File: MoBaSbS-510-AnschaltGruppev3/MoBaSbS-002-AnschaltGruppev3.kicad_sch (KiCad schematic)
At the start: 37 parts, among them IC1 TJA1057BT, IC2 SP3485EN-L_TR, IC3 MCP2518FDT-E_SL, J1 RJ45, J2 RJ45, J3 Conn_02x03_Odd_Even, J4 Conn_01x03, J5 Conn_02x05_Counter_Clockwise, J6 Conn_01x04, J7 Conn_01x04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

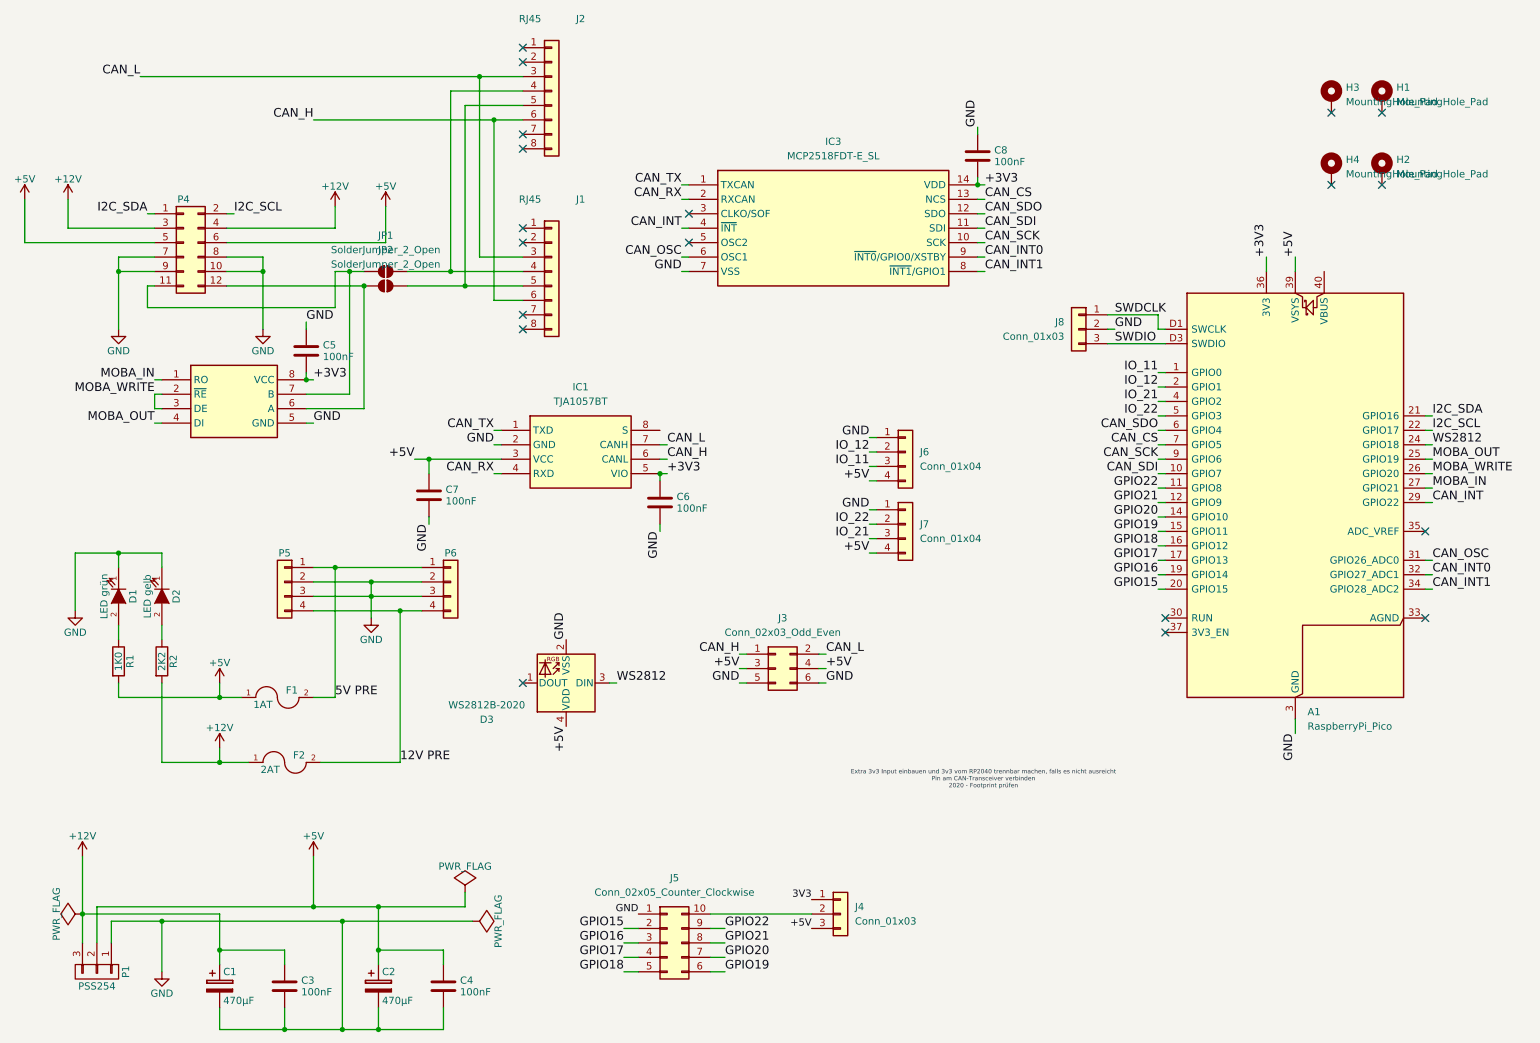
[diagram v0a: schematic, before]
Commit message: Finished up PCBs, added stencil
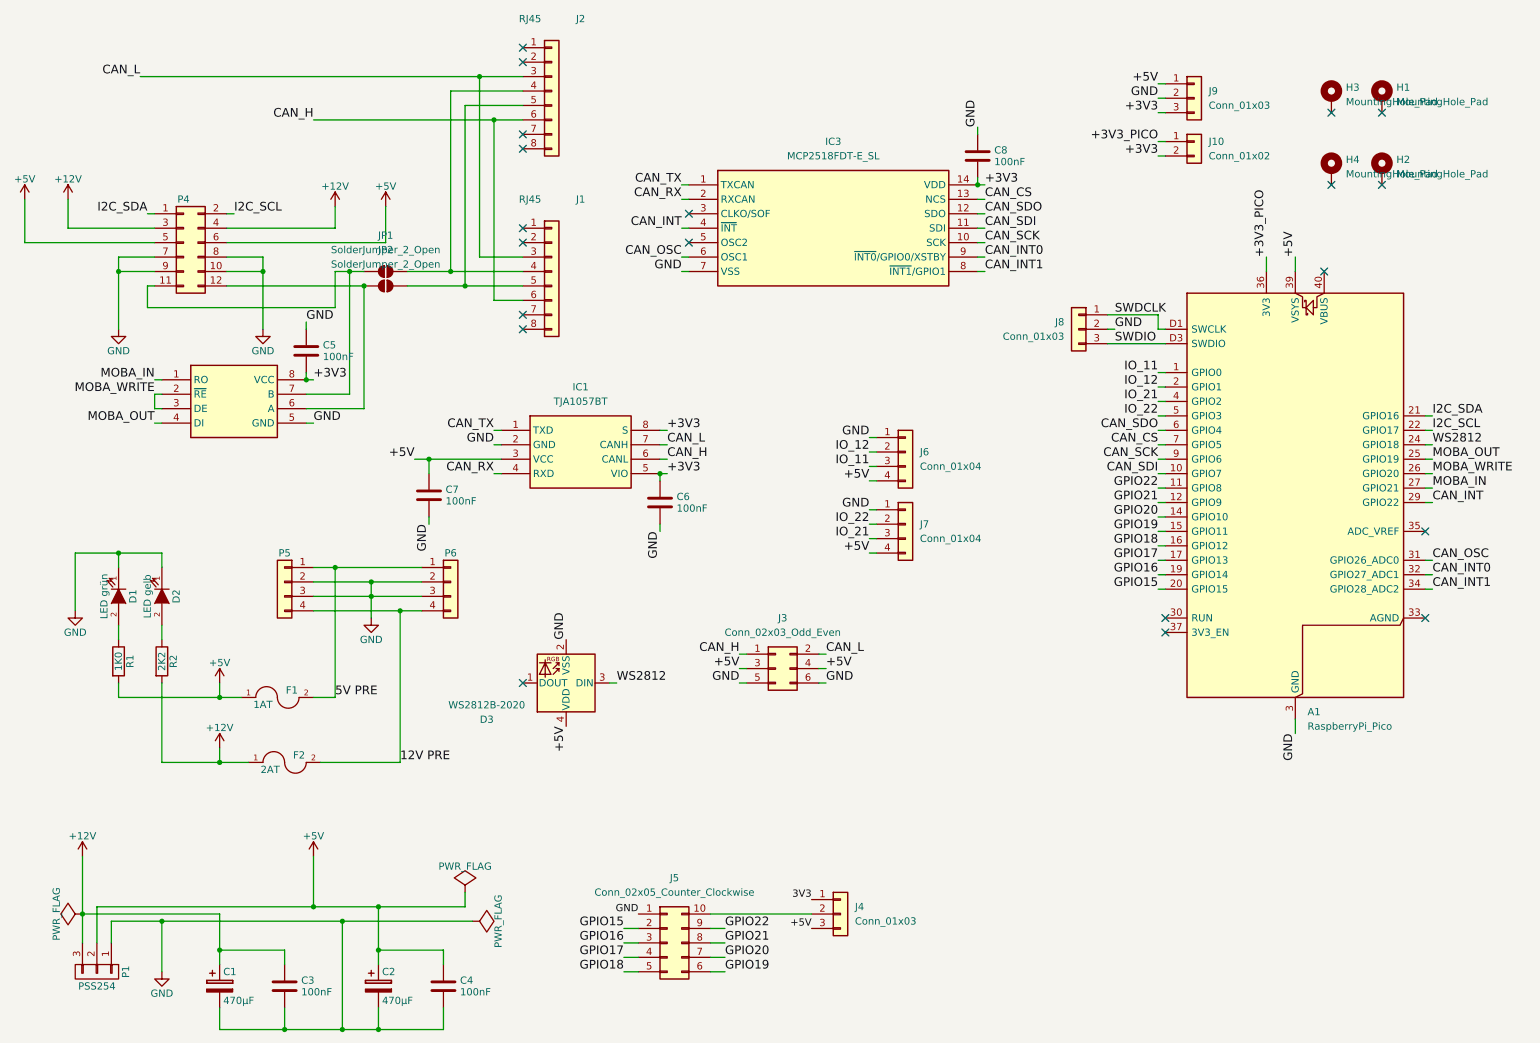
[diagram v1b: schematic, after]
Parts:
- added J10: Conn_01x02, Connector_PinHeader_2.54mm:PinHeader_1x02_P2.54mm_Vertical_SMD_Pin1Left, symbol Connector_Generic:Conn_01x02
- added J9: Conn_01x03, Connector_PinHeader_2.54mm:PinHeader_1x03_P2.54mm_Vertical_SMD_Pin1Left, symbol Connector_Generic:Conn_01x03
- D3: footprint LED_SMD:LED_WS2812B-2020_PLCC4_2.0x2.0mm -> LED_SMD:LED_WS2812B-Mini_PLCC4_3.5x3.5mm
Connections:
- net +3V3: now also IC1.8 (S), J10.2 (Pin_2), J9.3 (Pin_3); no longer A1.36 (3V3)
- net +5V: now also J9.1 (Pin_1)
- net GND: now also J9.2 (Pin_2)
- new net +3V3_PICO: A1.36 (3V3), J10.1 (Pin_1)
- no-connect marks 19 -> 20
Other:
- note removed: "Extra 3v3 Input einbauen und 3v3 vom RP2040 trennbar machen, falls es nicht ausreicht Pin am CAN-Transceiver verbinden 2020 - Footprint prüfen"

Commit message: Latest changes
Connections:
- net +3V3: no longer IC1.8 (S)
- net CAN_H: now also IC1.7 (CANH); no longer IC1.6 (CANL)
- net CAN_L: now also IC1.6 (CANL); no longer IC1.7 (CANH)
- net GND: now also IC1.8 (S)
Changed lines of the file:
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@@
+		)
+	)
+	(label "CAN_H"
+		(at 128.27 90.17 0)
+		(effects
+			(font
+				(size 1.524 1.524)
+			)
+			(justify left bottom)
 		)
 	)
@@
 		)
 	)
-	(label "CAN_H"
-		(at 128.27 92.71 0)
-		(effects
-			(font
-				(size 1.524 1.524)
-			)
-			(justify left bottom)
-		)
-	)
 	(label "CAN_L"
 		(at 35.56 25.4 180)
@@
 		)
 	)
+	(label "CAN_L"
+		(at 128.27 92.71 0)
+		(effects
+			(font
+				(size 1.524 1.524)
+			)
+			(justify left bottom)
+		)
+	)
 	(label "CAN_RX"
 		(at 97.79 95.25 180)
@@
 		)
 	)
-	(label "CAN_L"
-		(at 128.27 90.17 0)
-		(effects
-			(font
-				(size 1.524 1.524)
-			)
-			(justify left bottom)
-		)
-	)
 	(label "GPIO21"
 		(at 138.43 177.8 0)
@@
 		)
 	)
-	(label "+3V3"
-		(at 128.27 87.63 0)
-		(effects
-			(font
-				(size 1.524 1.524)
-			)
-			(justify left bottom)
-		)
-	)
 	(label "CAN_TX"
 		(at 97.79 87.63 180)
@@
 		)
 	)
+	(label "GND"
+		(at 128.27 87.63 0)
+		(effects
+			(font
+				(size 1.524 1.524)
+			)
+			(justify left bottom)
+		)
+	)
